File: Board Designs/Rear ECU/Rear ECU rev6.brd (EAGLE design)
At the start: 87.8 x 143.2 mm, 103 parts, among them X1 CONNECTOR-2, X3 CONNECTOR-10MX150L_VERTICAL-10, X4 CONNECTOR-10MX150L_VERTICAL-10

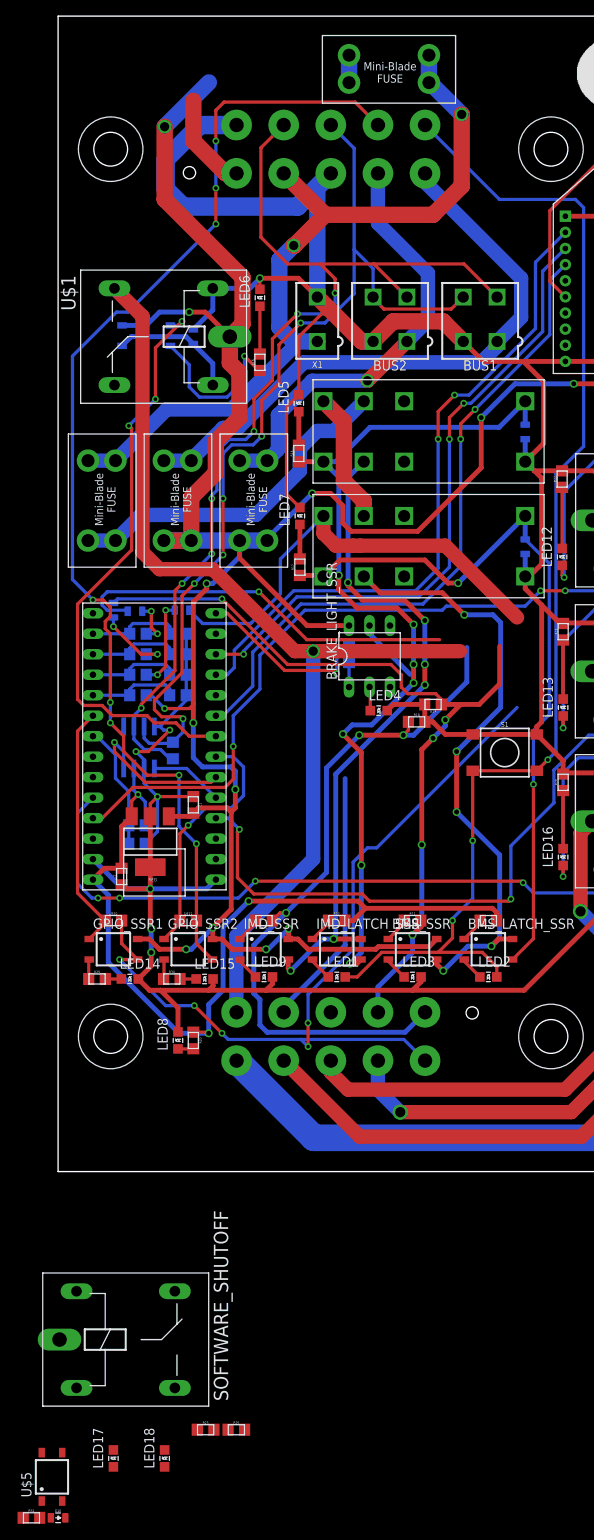
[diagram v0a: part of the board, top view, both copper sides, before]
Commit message: Init Front ECU rev8, Rear ECU rev6, from circuits-2018
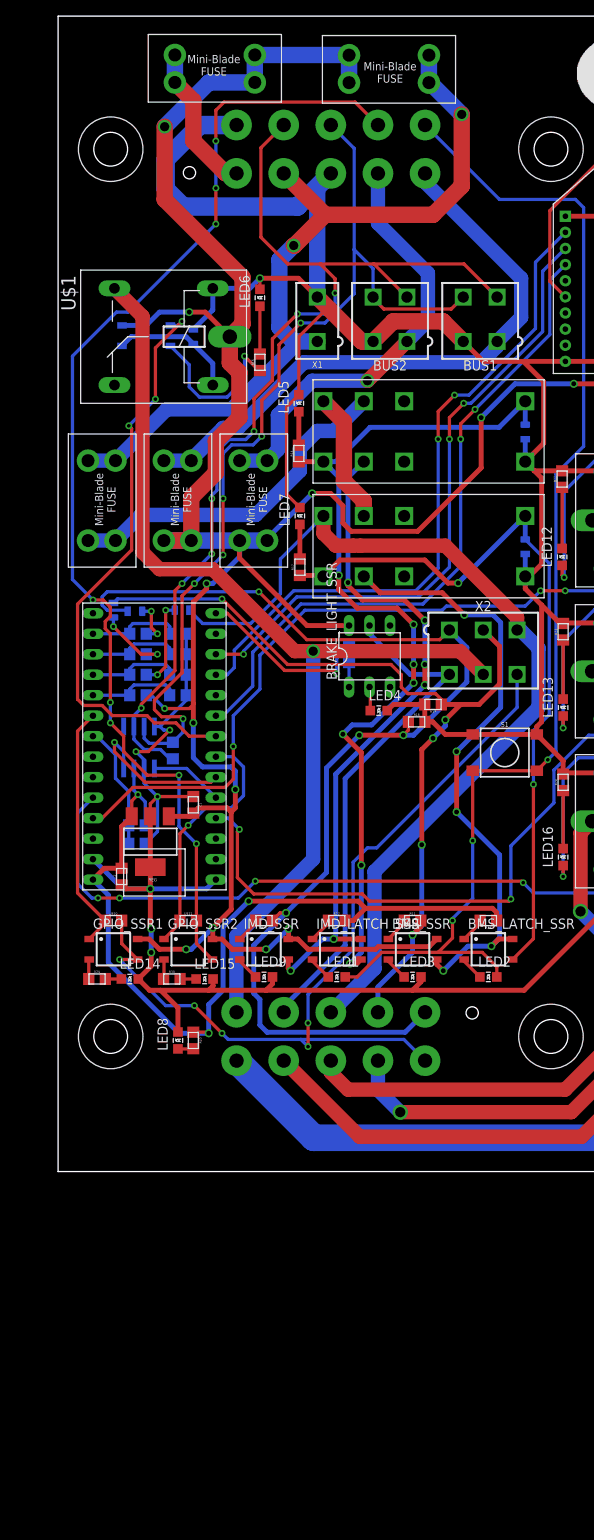
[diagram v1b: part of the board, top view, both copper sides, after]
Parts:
- removed D10: DIODE0805, HyTechDevices:0805_D
- removed LED17, LED18: RED, HyTechDevices:LED-805
- removed R25: 330, HyTechDevices:0805
- removed R26, R31: 1.2K, HyTechDevices:0805
- removed SOFTWARE_SHUTOFF: G5LE, HyTechDevices:ZF112
- removed U$5: CPC1002N, HyTechDevices:SOP04
- added FSAE_FUSE: 8A, HyTechDevices:MINI-BLADE_FUSE_HOLDER
- added X2: CONNECTOR-6, HyTechDevices:MINIFIT_5566-6
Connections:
- removed net N$40: LED18.A, R31.2
- removed net N$43: D10.C, R26.1, SOFTWARE_SHUTOFF.2, U$5.3
- removed net N$44: R25.2, U$5.2
- removed net N$46: LED17.A, R26.2
- removed net SHUTDOWN_D: R31.1, SOFTWARE_SHUTOFF.S, X3.3
- removed net SOFTWARE_SHUTDOWN: U$3.A7, U$5.1
- net +12V: now also FSAE_FUSE.L1, FSAE_FUSE.L2; no longer U$5.4
- net 12VSUPPLY_FSAE: now also FSAE_FUSE.R1, FSAE_FUSE.R2
- net BMS_OK: now also X2.2
- net BRAKE_LIGHT: now also X2.4
- net GND: no longer D10.A, LED17.C, LED18.C, R25.1, SOFTWARE_SHUTOFF.1
- net GPIO_1: now also X2.6
- net INVERTER_SUPPLY: now also X2.5
- net OKHS: now also X2.1
- net SHUTDOWN_C: now also X2.3, X3.3; no longer SOFTWARE_SHUTOFF.P
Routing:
- net SHUTDOWN_C: track 55.9 -> 116.8 mm
- net BRAKE_LIGHT: track 40.3 -> 63.4 mm
- net +12V: track 369.1 -> 389.8 mm
- net 12VSUPPLY_FSAE: track 12.0 -> 18.6 mm
- net OKHS: track 137.0 -> 141.7 mm
- net GPIO_1: track 107.6 -> 111.7 mm
- net INVERTER_SUPPLY: track 127.3 -> 131.4 mm
- net BMS_OK: track 105.1 -> 108.0 mm

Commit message: jparkerjones: Began updates on Front ECU, Moved Software Latch to Rear ECU
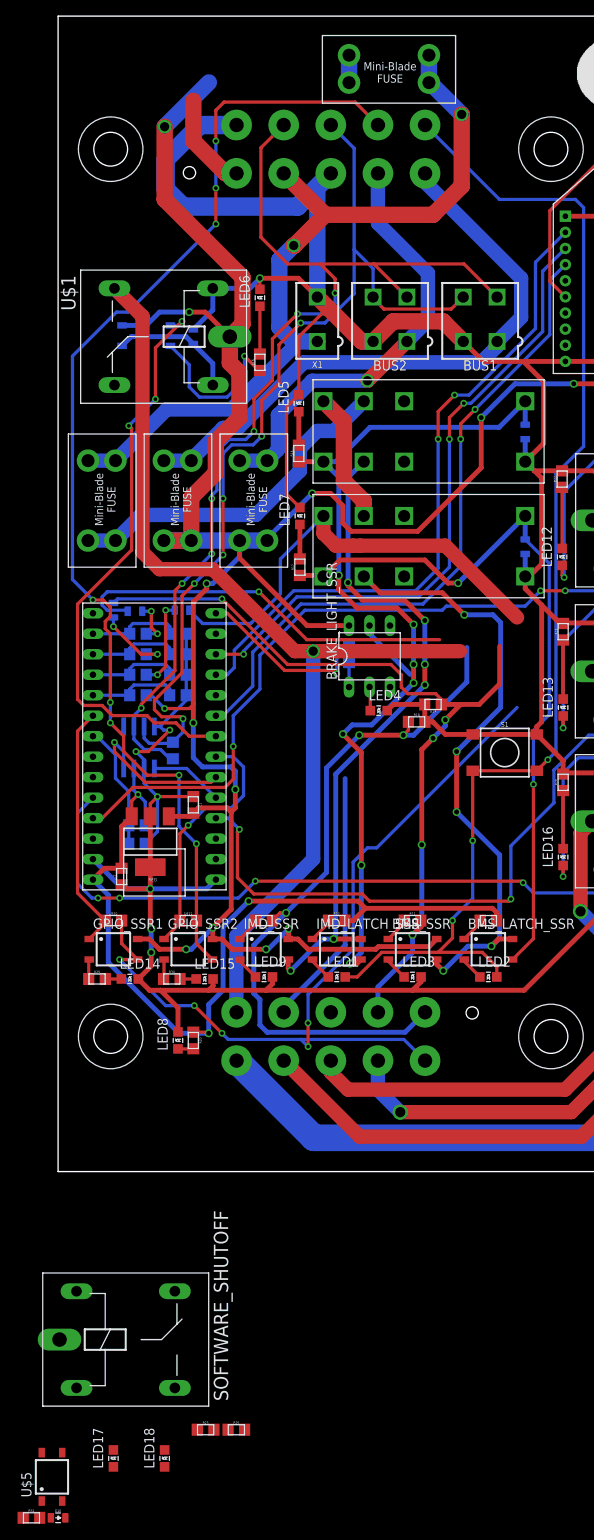
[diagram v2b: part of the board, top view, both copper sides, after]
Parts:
- removed FSAE_FUSE: 8A, HyTechDevices:MINI-BLADE_FUSE_HOLDER
- removed X2: CONNECTOR-6, HyTechDevices:MINIFIT_5566-6
- added D10: DIODE0805, HyTechDevices:0805_D
- added LED17, LED18: RED, HyTechDevices:LED-805
- added R25: 330, HyTechDevices:0805
- added R26, R31: 1.2K, HyTechDevices:0805
- added SOFTWARE_SHUTOFF: G5LE, HyTechDevices:ZF112
- added U$5: CPC1002N, HyTechDevices:SOP04
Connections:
- new net N$40: LED18.A, R31.2
- new net N$43: D10.C, R26.1, SOFTWARE_SHUTOFF.2, U$5.3
- new net N$44: R25.2, U$5.2
- new net N$46: LED17.A, R26.2
- new net SHUTDOWN_D: R31.1, SOFTWARE_SHUTOFF.S, X3.3
- new net SOFTWARE_SHUTDOWN: U$3.A7, U$5.1
- net +12V: now also U$5.4; no longer FSAE_FUSE.L1, FSAE_FUSE.L2
- net 12VSUPPLY_FSAE: no longer FSAE_FUSE.R1, FSAE_FUSE.R2
- net BMS_OK: no longer X2.2
- net BRAKE_LIGHT: no longer X2.4
- net GND: now also D10.A, LED17.C, LED18.C, R25.1, SOFTWARE_SHUTOFF.1
- net GPIO_1: no longer X2.6
- net INVERTER_SUPPLY: no longer X2.5
- net OKHS: no longer X2.1
- net SHUTDOWN_C: now also SOFTWARE_SHUTOFF.P; no longer X2.3, X3.3
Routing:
- net SHUTDOWN_C: track 116.8 -> 55.9 mm
- net BRAKE_LIGHT: track 63.4 -> 40.3 mm
- net +12V: track 389.8 -> 369.1 mm
- net 12VSUPPLY_FSAE: track 18.6 -> 12.0 mm
- net OKHS: track 141.7 -> 137.0 mm
- net GPIO_1: track 111.7 -> 107.6 mm
- net INVERTER_SUPPLY: track 131.4 -> 127.3 mm
- net BMS_OK: track 108.0 -> 105.1 mm

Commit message: Beginning work on Rear ECU
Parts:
- removed X4: CONNECTOR-10MX150L_VERTICAL-10, HyTechDevices:MX150L_VERTICAL-10
- X1: value CONNECTOR-2 -> CONNECTOR-8MX150L_RIGHT_ANGLE-8; device HyTechDevices:MINIFIT_5566-2 -> HyTechDevices:MX150L_RIGHT_ANGLE-8
- X3: value CONNECTOR-10MX150L_VERTICAL-10 -> CONNECTOR-10MX150L-RIGHT_ANGLE-10; device HyTechDevices:MX150L_VERTICAL-10 -> HyTechDevices:MX150L_RIGHT_ANGLE-10
- moved D10 152.4 mm to (-84.3, 84.1), flipped to the bottom, turned to 270 degrees
- moved R25 148.2 mm to (-84.3, 74.9), turned to 180 degrees
- moved U$5 144.5 mm to (-78.2, 84.1), flipped to the bottom, turned to 90 degrees
- moved R26 141.8 mm to (-68.3, 77.2)
- moved LED18 140.9 mm to (-78.2, 71.6), turned to 90 degrees
- moved R31 137.8 mm to (-75.2, 74.7), turned to 180 degrees
- moved R19 135.2 mm to (-88.1, 70.1)
- moved LED17 131.3 mm to (-72.1, 69.3)
- moved INVERTER_SSR 129.2 mm to (140.0, 96.5)
- moved SOFTWARE_SHUTOFF 125.2 mm to (39.6, 88.4), turned to 270 degrees
- moved X3 120.4 mm to (4.04, 133.4), turned to 180 degrees
- moved LED4 108.7 mm to (-47.1, -8.13)
- moved R18 108.1 mm to (-45.2, -4.70)
- moved U$2 104.1 mm to (4.57, 119.9), turned to 270 degrees
- moved R17 101.3 mm to (-70.4, 88.9)
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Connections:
- removed net 12VSUPPLY_FSAE: X4.1
- net 12VSUPPLY_BRB: now also X1.7; no longer X1.1, X4.2
- net 12V_F1: now also X1.3; no longer X4.5
- net 12V_F2: now also X1.2; no longer X4.4
- net CANH: now also X1.6; no longer X4.8
- net CANL: now also X1.5; no longer X4.7
- net GND: now also X1.1, X1.4; no longer X1.2, X4.3, X4.6
- net GPIO_2: no longer X4.9
- net LATCH_EXT_BUTTON: now also X1.8; no longer X4.10
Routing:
- net GND: track 507.2 -> 0.00 mm, vias 10 -> 0
- net +12V: track 369.1 -> 0.00 mm, vias 14 -> 0
- net LATCH_EXT_BUTTON: track 150.4 -> 0.00 mm, vias 3 -> 0
- net GPIO_2: track 145.9 -> 0.00 mm, vias 8 -> 0
- net OKHS: track 137.0 -> 0.00 mm, vias 4 -> 0
- net GND1: track 135.2 -> 0.00 mm
- net CANL: track 132.3 -> 0.00 mm, vias 7 -> 0
- net INVERTER_SUPPLY: track 127.3 -> 0.00 mm, vias 1 -> 0
- net CANH: track 119.4 -> 0.00 mm, vias 6 -> 0
- net PUMP1-: track 112.5 -> 0.00 mm, vias 1 -> 0
- net IMD_COIL_PWR: track 112.0 -> 0.00 mm, vias 7 -> 0
- net GPIO_1: track 107.6 -> 0.00 mm, vias 5 -> 0
- net BMS_OK: track 105.1 -> 0.00 mm, vias 5 -> 0
- net +5V: track 105.0 -> 0.00 mm, vias 3 -> 0
- net 12VSUPPLY_BRB: track 97.5 -> 0.00 mm, vias 2 -> 0
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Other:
- board size 87.8 x 143.2 mm -> 128.4 x 77.2 mm
- board text removed: "2018 Rear ECU rev5"
- board text removed: "Accum"
- board text removed: "Cherkbot approved"
- board text removed: "Designed by Nathan Cheek"
- board text removed: "FH Fuse"
- board text removed: "FSAE Fuse"
- board text removed: "Front"
- board text removed: "Inverter Power Relay"
- board text removed: "Shutdown"

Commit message: Inital Changes to Rear ECU Layout Completed
Teensy 3.5 added, Software Latch added, Right Angle Molex Connectors added
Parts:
- removed FH_FUSE: 8A, HyTechDevices:MINI-BLADE_FUSE_HOLDER
- removed GPIO_SSR2: CPC1002N, HyTechDevices:SOP04
- removed LED15: Red, HyTechDevices:LED-805
- removed R15: 120, HyTechDevices:0805
- removed R30: 43, HyTechDevices:0805
- removed U$11: JUMPER, HyTechDevices:0805
- removed U$3: TEENSY_3.2_SIMPLE, HyTechDevices:TEENSY_3.2_SIMPLE
- added U$4: TEENSY_3.5_EXT, HyTechDevices:TEENSY_3.5_EXT
- moved LED8 191.8 mm to (125.7, 91.1)
- moved R20 187.7 mm to (121.4, 91.2), turned to 0 degrees
- moved FUSE_BUS_2 182.5 mm to (109.5, 118.9)
- moved R9 151.9 mm to (122.9, 73.3), turned to 90 degrees
- moved BOARD_TEMP 151.8 mm to (122.9, 77.6), turned to 270 degrees
- moved C2 145.7 mm to (115.3, 89.9), flipped to the bottom, turned to 270 degrees
- moved R17 144.9 mm to (74.3, 96.9), turned to 180 degrees
- moved S1 140.3 mm to (93.1, 89.4), turned to 180 degrees
- moved D10 136.2 mm to (51.8, 89.4), turned to 90 degrees
- moved R25 134.6 mm to (49.8, 86.6), flipped to the bottom, turned to 0 degrees
- moved R18 134.5 mm to (20.1, 112.9), flipped to the bottom, turned to 180 degrees
- moved LED17 133.9 mm to (58.2, 100.3), turned to 270 degrees
- moved REG 132.3 mm to (105.7, 89.7), flipped to the bottom, turned to 270 degrees
- moved U$10 129.1 mm to (52.1, 72.3)
- moved LED1 128.9 mm to (79.0, 94.2)
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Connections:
- removed net GPIO_2: GPIO_SSR2.3, U$11.2
- removed net GPIO_CTRL2: GPIO_SSR2.1, U$11.1, U$3.D5
- removed net N$14: LED15.A, R30.2
- removed net N$8: GPIO_SSR2.2, R30.1
- net +12V: no longer FH_FUSE.L1, FH_FUSE.L2, GPIO_SSR2.4
- net +5V: now also U$4.VIN; no longer U$3.VIN
- net 12VSUPPLY_BRB: no longer FH_FUSE.R1, FH_FUSE.R2
- net 12VSUPPLY_READ: now also U$4.A3; no longer U$3.A3
- net BMS_OK_READ: now also U$4.A1; no longer U$3.A1
- net BRAKE_LIGHT_CTRL: now also U$4.D12; no longer U$3.D12
- net CANH: no longer R15.1
- net CANL: no longer R15.2
- net GND: now also U$4.AGND, U$4.GND; no longer LED15.C, U$3.AGND, U$3.GND
- net GPIO_CTRL1: now also U$4.A4; no longer U$3.A4
- net INVERTER_CTRL: now also U$4.D6; no longer U$3.D6
- net N$15: now also U$4.A5; no longer U$3.A5
- net N$2: now also U$4.D4(CANRX); no longer U$3.D4(CANRX)
- net N$3: now also U$4.D3(CANTX); no longer U$3.D3(CANTX)
- net OKHS_READ: now also U$4.A0; no longer U$3.A0
- net RELAY_CTRL1: now also U$4.A9; no longer U$3.A9
- net RELAY_CTRL2: now also U$4.D2; no longer U$3.D2
- net RELAY_CTRL3: now also U$4.A8; no longer U$3.A8
- net SHUTDOWN_OUT_READ: now also U$4.A2; no longer U$3.A2
- net SOFTWARE_SHUTDOWN: now also U$4.A7; no longer U$3.A7
- net XB8: now also U$4.D7(RX3); no longer U$3.D7(RX3)
- net XBDI: now also U$4.D10(TX2); no longer U$3.D10(TX2)
- net XBDO: now also U$4.D9(RX2); no longer U$3.D9(RX2)
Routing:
- net GND: track 0.00 -> 553.0 mm, vias 0 -> 5
- net +12V: track 0.00 -> 289.0 mm, vias 0 -> 8
- net OKHS: track 0.00 -> 151.7 mm, vias 0 -> 4
- net BMS_OK: track 0.00 -> 133.7 mm, vias 0 -> 2
- net RELAY_CTRL1: track 0.00 -> 125.3 mm, vias 0 -> 1
- net RELAY_CTRL2: track 0.00 -> 119.1 mm, vias 0 -> 1
- net BRAKE_LIGHT_CTRL: track 0.00 -> 108.4 mm, vias 0 -> 1
- net XBDO: track 0.00 -> 107.4 mm, vias 0 -> 3
- net XB8: track 0.00 -> 105.9 mm, vias 0 -> 3
- net XBDI: track 0.00 -> 104.4 mm, vias 0 -> 3
- net RELAY_CTRL3: track 0.00 -> 102.5 mm, vias 0 -> 1
- net IMD_COIL_PWR: track 0.00 -> 93.3 mm, vias 0 -> 2
- net GPIO_1: track 0.00 -> 88.1 mm, vias 0 -> 3
- net +5V: track 0.00 -> 85.6 mm, vias 0 -> 3
- net SOFTWARE_SHUTDOWN: track 0.00 -> 83.5 mm, vias 0 -> 1
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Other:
- board size 128.4 x 77.2 mm -> 128.4 x 78.7 mm
